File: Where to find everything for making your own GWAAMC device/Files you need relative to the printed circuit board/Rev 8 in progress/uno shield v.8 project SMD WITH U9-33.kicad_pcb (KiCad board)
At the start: 2 copper layers, 68.6 x 53.3 mm, 82 parts, among them J1 Conn_3.5mm, J2 Power, J3 Analog, J4 Digital, J5 Digital, J6 Conn_01x09_Female, J6_A7,A6 Conn_01x02_gender_unknown, J7_A7,A6 Conn_01x02_Female, J9 TE_1-2328702-0, P1 CONN_01X01, P2 CONN_01X01, P3 CONN_01X01, P4 CONN_01X01, Q1 MMBF5460 (2N5460), Q2 MMBF5460 (2N5460), Q3 DMN601K-7, Q4 DMN601K-7, Q5 DMN601K-7, Q6 DMN601K-7, Q7 DMN601K-7, U1 3V LDO, U2 AD8244ARMZ, U3 ADL5315ACPZ-R7, U4 REF200AU, U5 LM334M, U6 LM334M, U7 MCP4262-503E/UN, U8 - U32 all in parallel MCP4262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

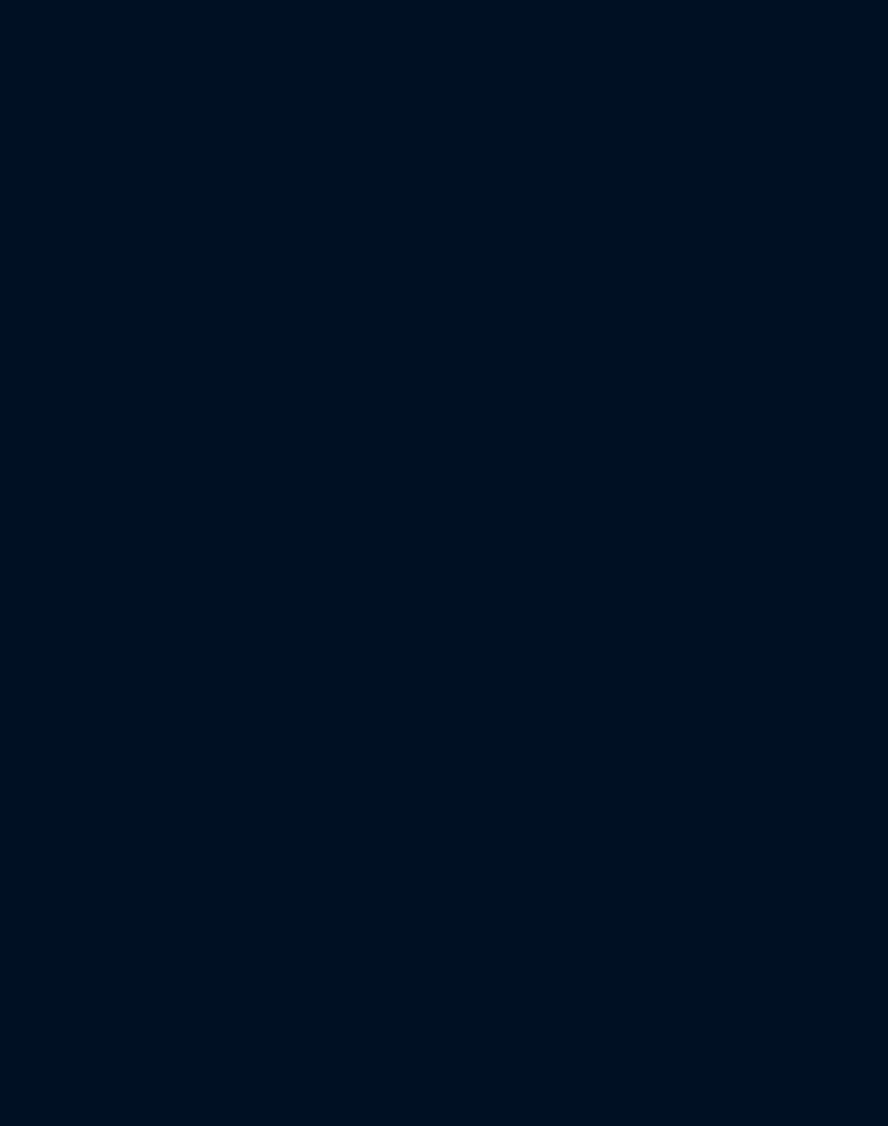
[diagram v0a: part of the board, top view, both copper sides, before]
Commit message: In the latest state of progress...
I HAVEN'T DESIGNED THE FLEX CIRCUIT BOARD FOR U9-U33, THE PARALLELED MCP4262-502 DPOTS, BUT THE REST OF THESE FILES ARE COMPLETED AND FUNCTIONAL TO THE BEST OF MY UNDERSTANDING, INCLUDING THE MAIN BOARD BEING COMPLETE AND WORKING.
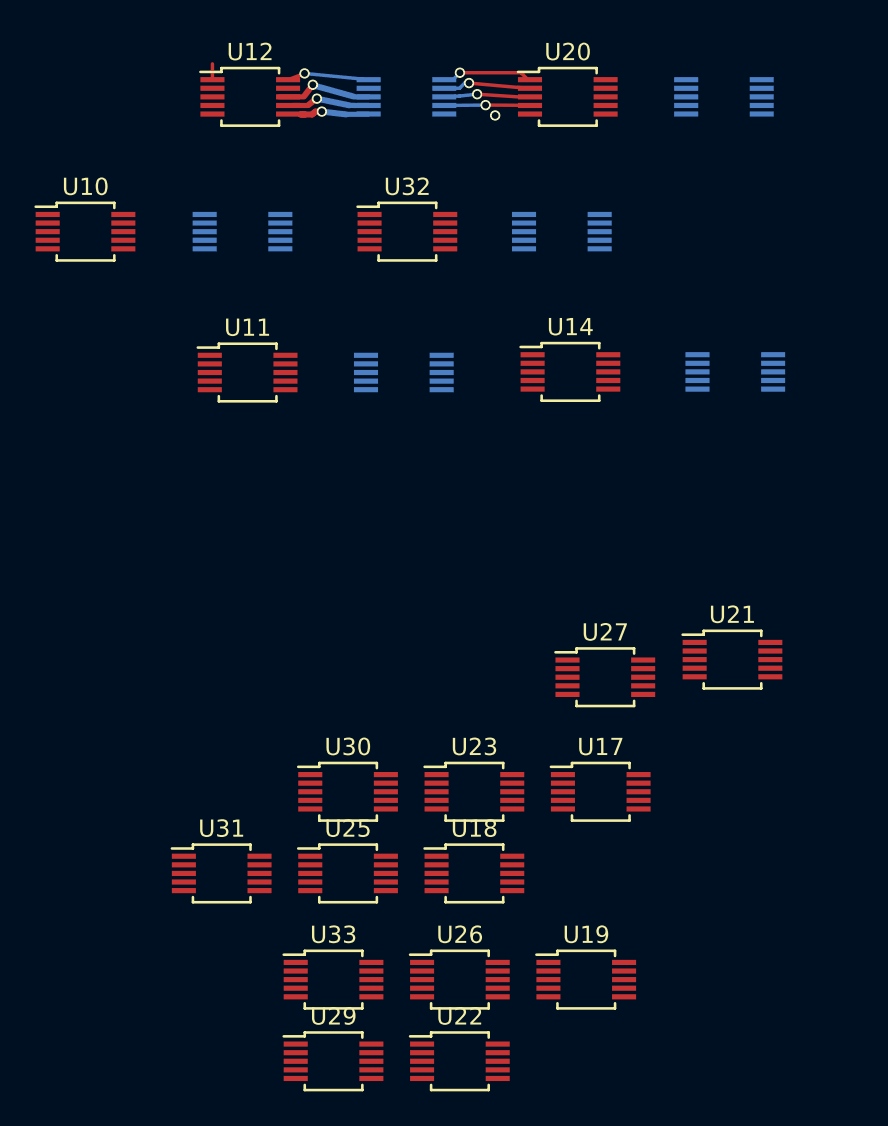
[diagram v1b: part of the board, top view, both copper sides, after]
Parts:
- added U10: MCP4262-502E/UN, Package_SO:MSOP-10_3x3mm_P0.5mm, F.Cu at (-64.9, 85.8)
- added U11: MCP4262-502E/UN, Package_SO:MSOP-10_3x3mm_P0.5mm, F.Cu at (-55.4, 93.9)
- added U12: MCP4262-502E/UN, Package_SO:MSOP-10_3x3mm_P0.5mm, F.Cu at (-55.3, 77.9)
- added U13: MCP4262-502E/UN, Package_SO:MSOP-10_3x3mm_P0.5mm, B.Cu at (-46.4, 93.9)
- added U14: MCP4262-502E/UN, Package_SO:MSOP-10_3x3mm_P0.5mm, F.Cu at (-36.7, 93.9)
- added U15: MCP4262-502E/UN, Package_SO:MSOP-10_3x3mm_P0.5mm, B.Cu at (-27.1, 93.9)
- added U16: MCP4262-502E/UN, Package_SO:MSOP-10_3x3mm_P0.5mm, B.Cu at (-46.2, 77.9)
- added U17: MCP4262-502E/UN, Package_SO:MSOP-10_3x3mm_P0.5mm, F.Cu at (-34.9, 118.3)
- added U18: MCP4262-502E/UN, Package_SO:MSOP-10_3x3mm_P0.5mm, F.Cu at (-42.3, 123.1)
- added U19: MCP4262-502E/UN, Package_SO:MSOP-10_3x3mm_P0.5mm, F.Cu at (-35.8, 129.3)
- added U20: MCP4262-502E/UN, Package_SO:MSOP-10_3x3mm_P0.5mm, F.Cu at (-36.8, 77.9)
- added U21: MCP4262-502E/UN, Package_SO:MSOP-10_3x3mm_P0.5mm, F.Cu at (-27.2, 110.7)
- added U22: MCP4262-502E/UN, Package_SO:MSOP-10_3x3mm_P0.5mm, F.Cu at (-43.1, 134.0)
- added U23: MCP4262-502E/UN, Package_SO:MSOP-10_3x3mm_P0.5mm, F.Cu at (-42.3, 118.3)
- added U24: MCP4262-502E/UN, Package_SO:MSOP-10_3x3mm_P0.5mm, B.Cu at (-27.7, 77.9)
- added U25: MCP4262-502E/UN, Package_SO:MSOP-10_3x3mm_P0.5mm, F.Cu at (-49.6, 123.1)
- added U26: MCP4262-502E/UN, Package_SO:MSOP-10_3x3mm_P0.5mm, F.Cu at (-43.1, 129.3)
- added U27: MCP4262-502E/UN, Package_SO:MSOP-10_3x3mm_P0.5mm, F.Cu at (-34.6, 111.7)
- added U28: MCP4262-502E/UN, Package_SO:MSOP-10_3x3mm_P0.5mm, B.Cu at (-37.2, 85.8)
- added U29: MCP4262-502E/UN, Package_SO:MSOP-10_3x3mm_P0.5mm, F.Cu at (-50.5, 134.0)
- added U30: MCP4262-502E/UN, Package_SO:MSOP-10_3x3mm_P0.5mm, F.Cu at (-49.6, 118.3)
- added U31: MCP4262-502E/UN, Package_SO:MSOP-10_3x3mm_P0.5mm, F.Cu at (-57.0, 123.1)
- added U32: MCP4262-502E/UN, Package_SO:MSOP-10_3x3mm_P0.5mm, F.Cu at (-46.2, 85.8)
- added U33: MCP4262-502E/UN, Package_SO:MSOP-10_3x3mm_P0.5mm, F.Cu at (-50.5, 129.3)
- added U9: MCP4262-502E/UN, Package_SO:MSOP-10_3x3mm_P0.5mm, B.Cu at (-55.7, 85.8)
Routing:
- net /8: track 44.3 -> 50.3 mm, vias 4 -> 5
- net /U8-Pad8: track 12.6 -> 18.2 mm, vias 1 -> 2
- net /SCK(1): track 16.1 -> 21.2 mm, vias 1 -> 2
- net +5V: track 246.3 -> 251.1 mm, vias 28 -> 29
- net /U8-Pad7: track 14.3 -> 19.1 mm, vias 1 -> 2
- net GNDD: track 204.4 -> 208.8 mm, vias 41 -> 42
- net /MOSI(1): track 17.8 -> 22.2 mm, vias 1 -> 2
- net /U8-Pad6: track 28.0 -> 32.3 mm, vias 3 -> 4
- net (no net): vias 0 -> 1
